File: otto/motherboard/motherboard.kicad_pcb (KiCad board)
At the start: 2 copper layers, 60 x 60 mm, 13 parts, among them J1 ServoGauche4, J10 ServoDroit4, J2 Battery, J3 ServoGauche3, J4 ServoDroit2, J5 ServoDroit1, J6 Ultrasons, J7 ServoGauche2, J8 ServoGauche1, J9 ServoDroit3

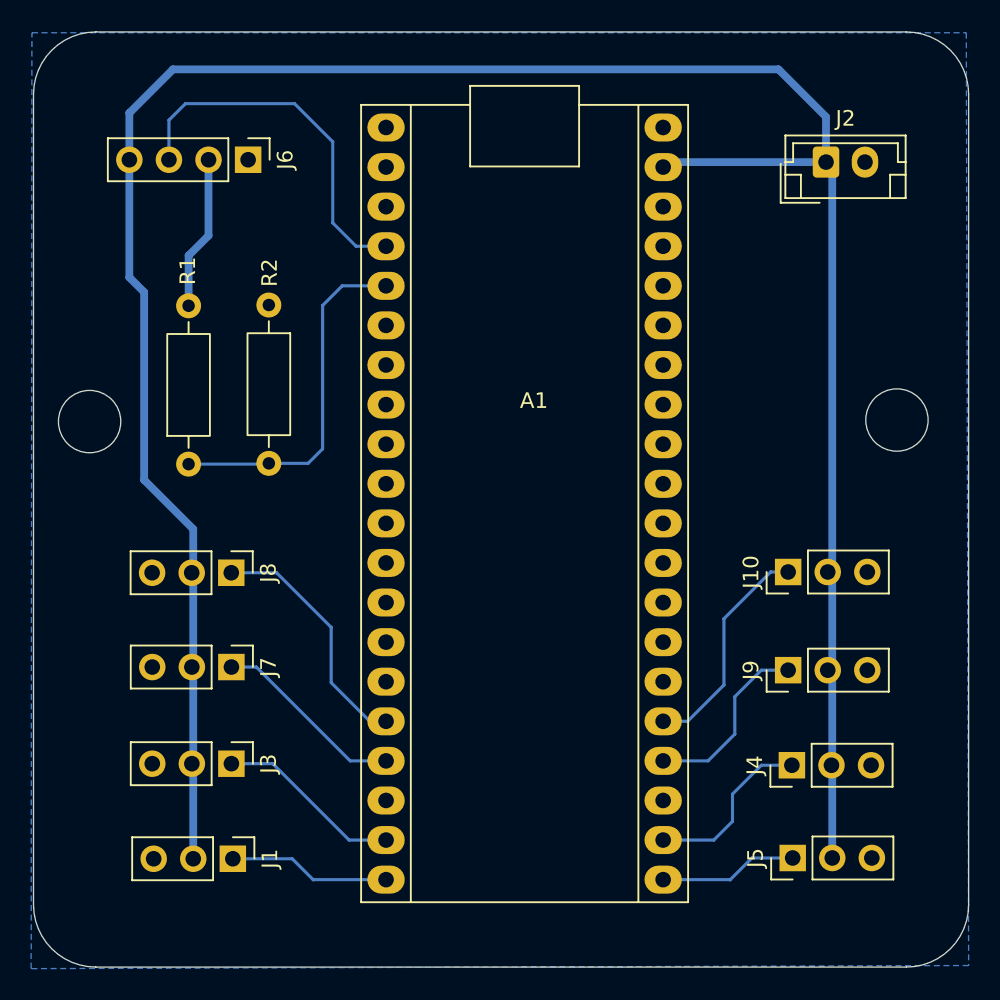
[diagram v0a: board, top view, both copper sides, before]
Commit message: adds otto mb and pico servo code
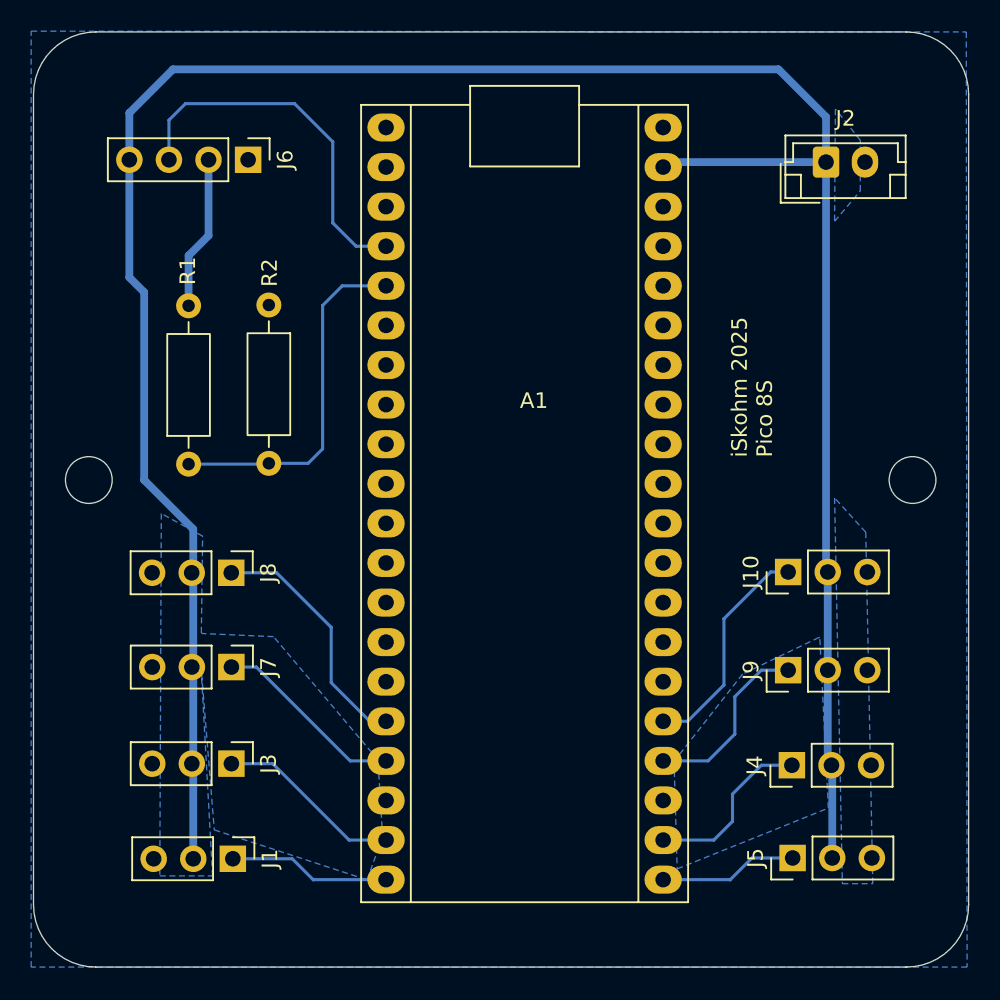
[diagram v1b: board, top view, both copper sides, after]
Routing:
- net /5V: track 155.0 -> 155.7 mm
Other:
- outline, holes or cut-outs redrawn
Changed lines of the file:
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@@
 			(drillshape 0)
 			(scaleselection 1)
-			(outputdirectory "./")
+			(outputdirectory "gerbers/")
 		)
 	)
@@
 		)
 		(property "Value" "Battery"
-			(at 1.25 3.4 0)
+			(at 6.65 0.4 270)
 			(layer "F.Fab")
 			(effects
@@
 		)
 		(property "Value" "Ultrasons"
-			(at 0 10 90)
+			(at 0.3 10.62 90)
 			(layer "F.Fab")
 			(effects
@@
 	)
 	(gr_circle
-		(center 123.75 94.95)
-		(end 125.75 94.95)
+		(center 123.7 98.7)
+		(end 125.2 98.7)
 		(stroke
 			(width 0.05)
@@
 	)
 	(gr_circle
-		(center 175.55 94.85)
-		(end 177.55 94.85)
+		(center 176.55 98.7)
+		(end 178.05 98.7)
 		(stroke
 			(width 0.05)
@@
 	)
 	(gr_text "iSkohm 2025\nPico 8S"
-		(at 146.9 129.2 0)
-		(layer "Edge.Cuts")
+		(at 167.65 97.25 90)
+		(layer "F.SilkS")
 		(effects
 			(font
@@
 	)
 	(segment
+		(start 171 104.49)
+		(end 171.11 104.6)
+		(width 0.5)
+		(layer "B.Cu")
+		(net 3)
+	)
+	(segment
 		(start 130.4 101.85)
 		(end 130.4 123)
@@
 	)
 	(segment
+		(start 171.4 117.05)
+		(end 171.35 117)
+		(width 0.5)
+		(layer "B.Cu")
+		(net 3)
+	)
+	(segment
 		(start 171 78.3)
 		(end 171 78.45)
@@
 	)
 	(segment
+		(start 171.11 110.9)
+		(end 171.11 116.76)
+		(width 0.5)
+		(layer "B.Cu")
+		(net 3)
+	)
+	(segment
+		(start 171 78.3)
+		(end 171 104.49)
+		(width 0.5)
+		(layer "B.Cu")
+		(net 3)
+	)
+	(segment
 		(start 171 78.45)
 		(end 171.4 78.85)
@@
 	)
 	(segment
+		(start 171.4 122.95)
+		(end 171.4 117.05)
+		(width 0.5)
+		(layer "B.Cu")
+		(net 3)
+	)
+	(segment
 		(start 127.25 98.7)
 		(end 130.4 101.85)
@@
 	)
 	(segment
-		(start 171.4 78.85)
-		(end 171.4 122.95)
+		(start 126.3 85.7)
+		(end 127.25 86.65)
 		(width 0.5)
 		(layer "B.Cu")
@@
 	)
 	(segment
-		(start 126.3 85.7)
-		(end 127.25 86.65)
+		(start 171.11 116.76)
+		(end 171.35 117)
+		(width 0.5)
+		(layer "B.Cu")
+		(net 3)
+	)
+	(segment
+		(start 171.11 104.6)
+		(end 171.11 110.9)
 		(width 0.5)
 		(layer "B.Cu")
@@
 		(filled_areas_thickness no)
 		(fill yes
-			(thermal_gap 0.5)
-			(thermal_bridge_width 0.5)
+			(thermal_gap 0.4)
+			(thermal_bridge_width 0.7)
+		)
+		(polygon
+			(pts
+				(xy 180 69.95) (xy 180.05 129.95) (xy 120 129.95) (xy 120 69.9)
+			)
+		)
+		(polygon
+			(pts
+				(xy 128.254518 124.1) (xy 131.639311 124.1) (xy 130.891886 110.552641) (xy 131.75 121.15) (xy 141.55 124.35)
+				(xy 142.55 121.6) (xy 142.25 116.65) (xy 135.55 108.75) (xy 131 108.55) (xy 130.918655 108.509327)
+				(xy 131 102.3) (xy 128.35 100.85)
+			)
+		)
+		(polygon
+			(pts
+				(xy 171.55 99.85) (xy 172.05 124.6) (xy 174 124.6) (xy 173.55 102.05)
+			)
+		)
+		(polygon
+			(pts
+				(xy 165.65 111.15) (xy 161.25 116.75) (xy 161.45 123.65) (xy 171.15 119.75) (xy 170.6 108.8) (xy 170.55 108.8)
+			)
 		)
 		(polygon
 			(pts
-				(xy 120.05 70) (xy 180 70) (xy 180.15 129.85) (xy 120 130.05)
+				(xy 171.55 82.1) (xy 173.2 80.15) (xy 173.2 76.9) (xy 171.65 74.95) (xy 171.6 74.9)
 			)
 		)
